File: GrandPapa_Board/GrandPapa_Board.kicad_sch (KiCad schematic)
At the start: 0 parts

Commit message: Shameless papa copying pt 1
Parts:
- added J? (x3): M80-5000642, Payload2020_custom:connector_Harwin_M80-5000642, symbol Connector_Generic:Conn_02x03_Counter_Clockwise
- added J?: Conn_02x06, Connector_PinHeader_2.54mm:PinHeader_1x05_P2.54mm_Vertical, symbol Connector:Conn_01x05_Female
- added J?: Conn_01x02_Female, symbol Connector:Conn_01x02_Female
- added J?: Conn_02x06, Payload2020_custom:connector_Harwin_M80-5000642, symbol Connector_Generic:Conn_01x05
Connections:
- new net +3V3: J?.4 (Pin_4)
- new net CANH_PAYLOAD: J?.4 (Pin_4), J?.4 (Pin_4), J?.4 (Pin_4)
- new net CANH_ROCKET: J?.4 (Pin_4)
- new net CANL_PAYLOAD: J?.5 (Pin_5), J?.5 (Pin_5), J?.5 (Pin_5)
- new net CANL_ROCKET: J?.5 (Pin_5)
- new net GND: J?.3 (Pin_3), J?.3 (Pin_3), J?.3 (Pin_3), J?.3 (Pin_3), J?.3 (Pin_3)
- new net ICSPCLK: J?.1 (Pin_1)
- new net ICSPDAT: J?.2 (Pin_2)
- new net ~{MCLR}: J?.5 (Pin_5)
- no-connect marks 0 -> 5
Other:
- note added: "Connector for programming"
- note added: "GPS Board"
- note added: "Harwin connector"
- note added: "Logger Board"
- note added: "Minisesnor Board"
- note added: "Motor CTRL"
- note added: "Normal header"
- note added: "To Rocket CAN bus"

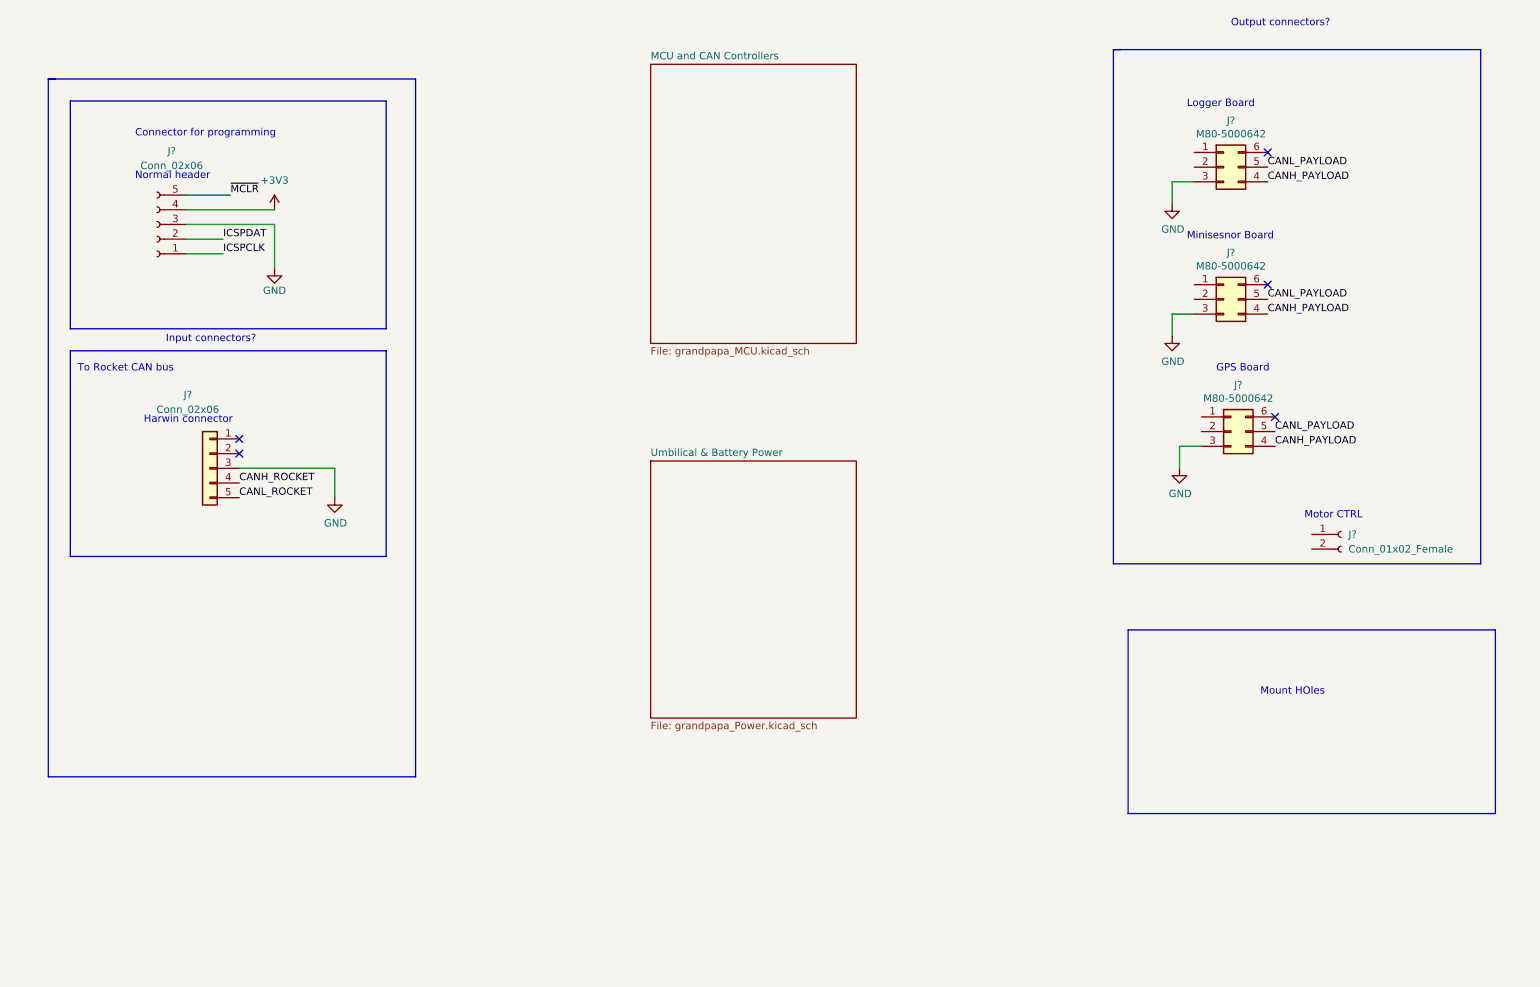
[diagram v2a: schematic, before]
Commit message: Add missing capacitor value, annotate symbols
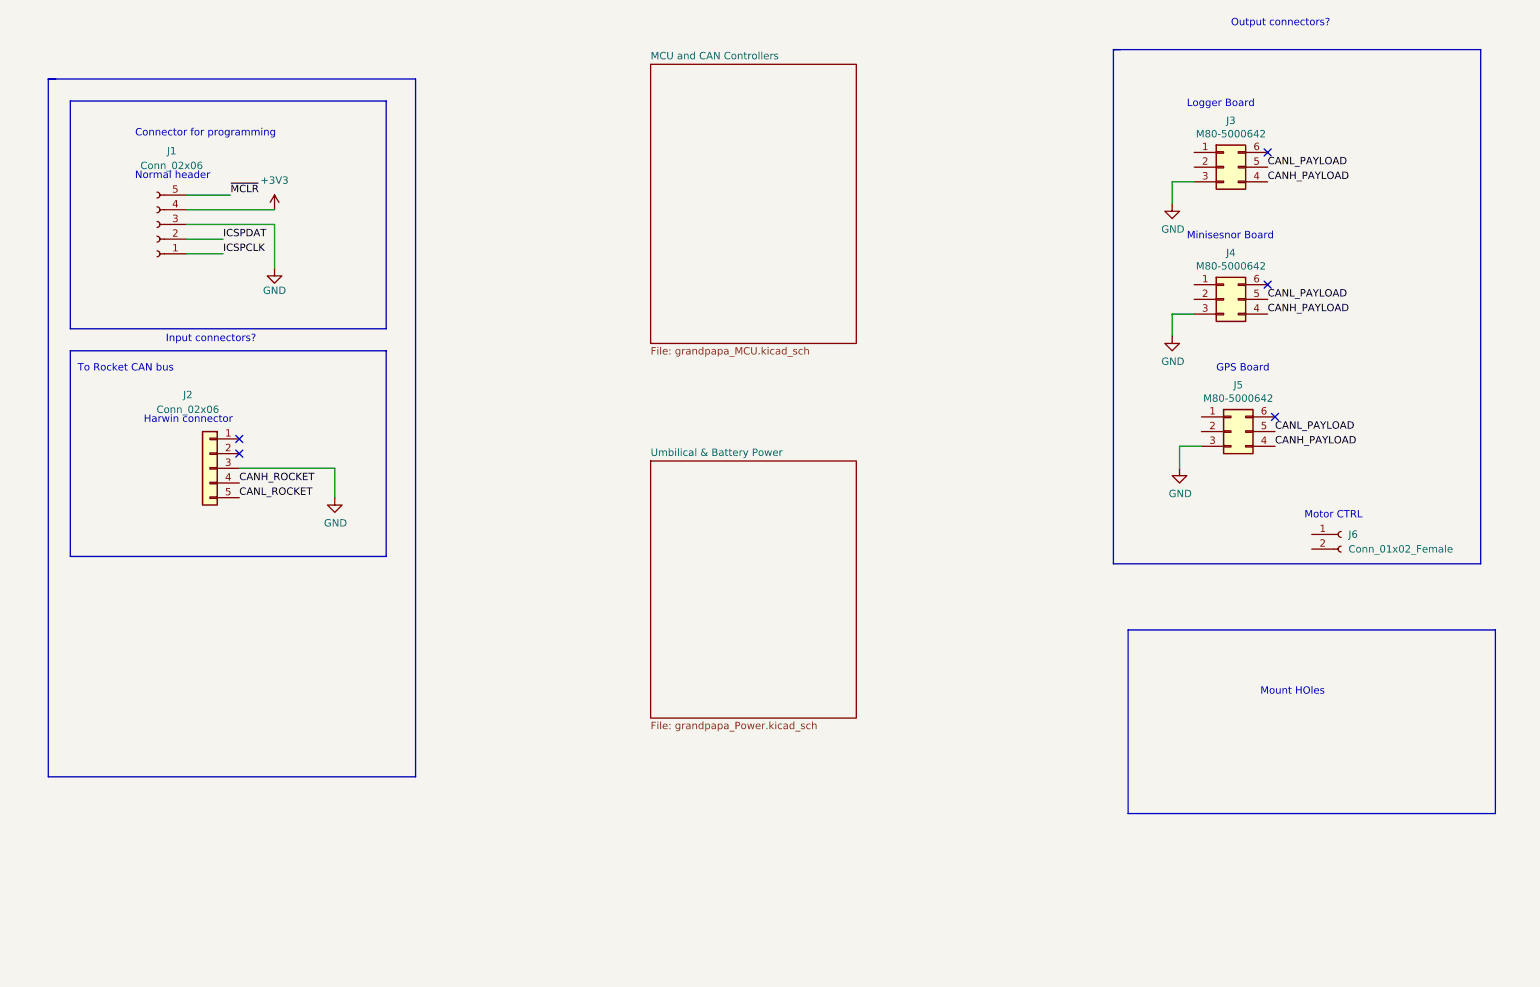
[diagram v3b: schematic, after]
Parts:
- gave numbers to parts that had none: 6

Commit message: Add motor current sense amp and board output connections
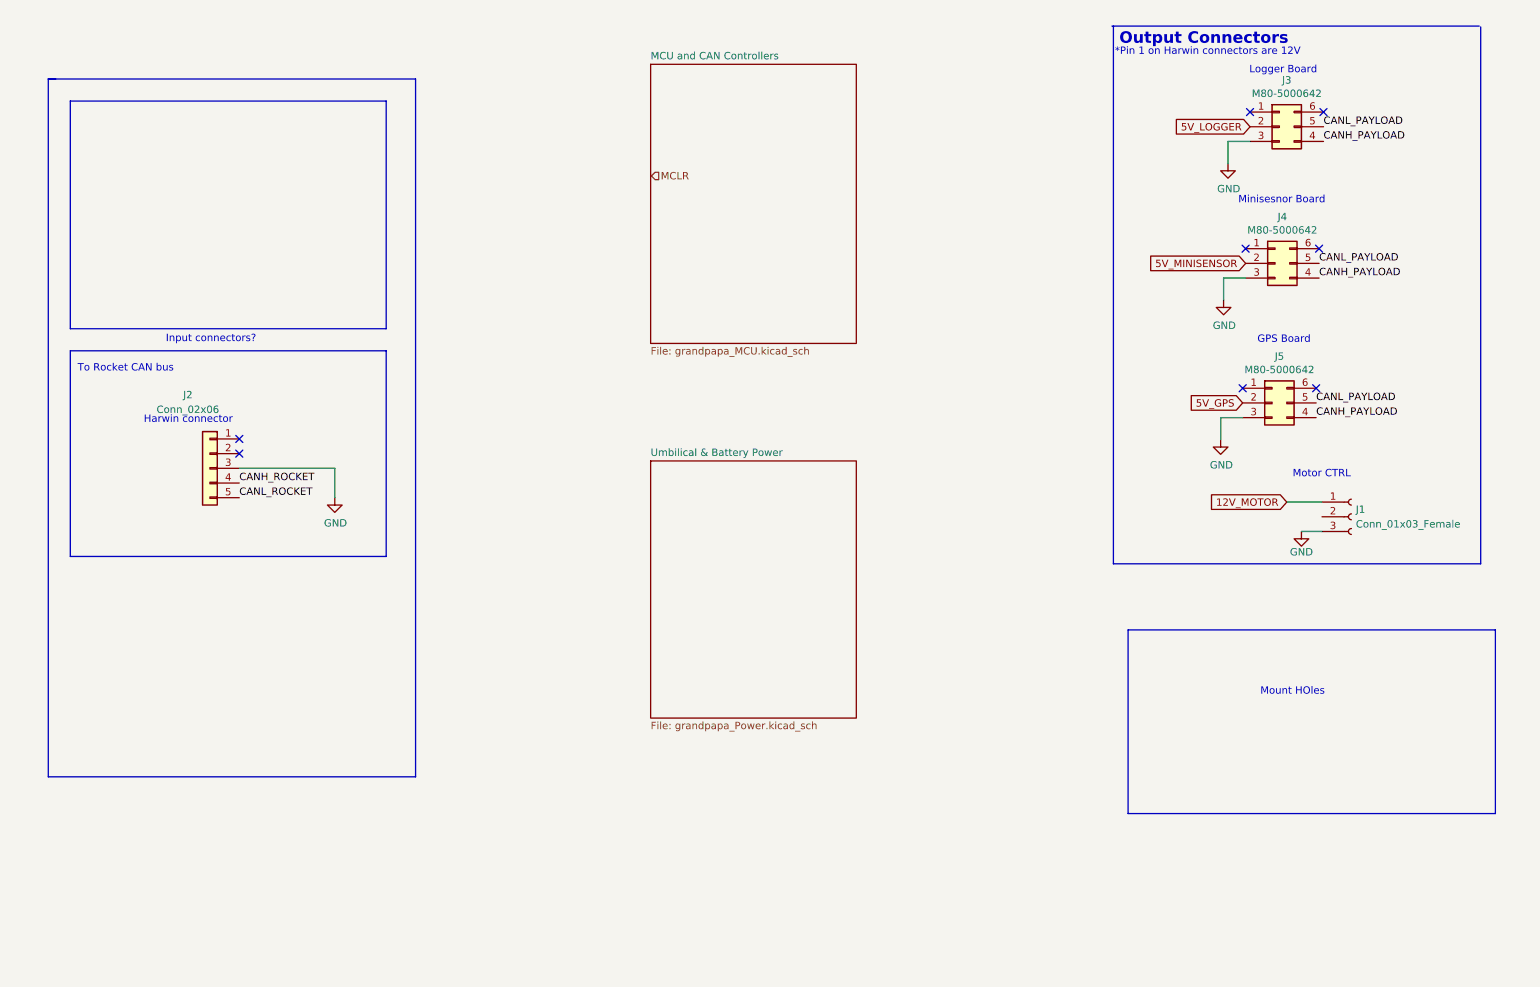
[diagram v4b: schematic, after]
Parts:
- removed J1: Conn_02x06, Connector_PinHeader_2.54mm:PinHeader_1x05_P2.54mm_Vertical, symbol Connector:Conn_01x05_Female
- removed J6: Conn_01x02_Female, symbol Connector:Conn_01x02_Female
- added J1: Conn_01x03_Female, symbol Connector:Conn_01x03_Female
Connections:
- net GND: now also J1.3 (Pin_3)
- net 5V_LOGGER: now reaches J3.2 (Pin_2)
- net 5V_GPS: now reaches J5.2 (Pin_2)
- net 5V_MINISENSOR: now reaches J4.2 (Pin_2)
- new net 12V_MOTOR: J1.1 (Pin_1)
- no-connect marks 5 -> 8
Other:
- note added: "*Pin 1 on Harwin connectors are 12V"
- note added: "Output Connectors"
- note removed: "Connector for programming"
- note removed: "Normal header"
- note removed: "Output connectors?"
- moved on the sheet: J3, J4, J5

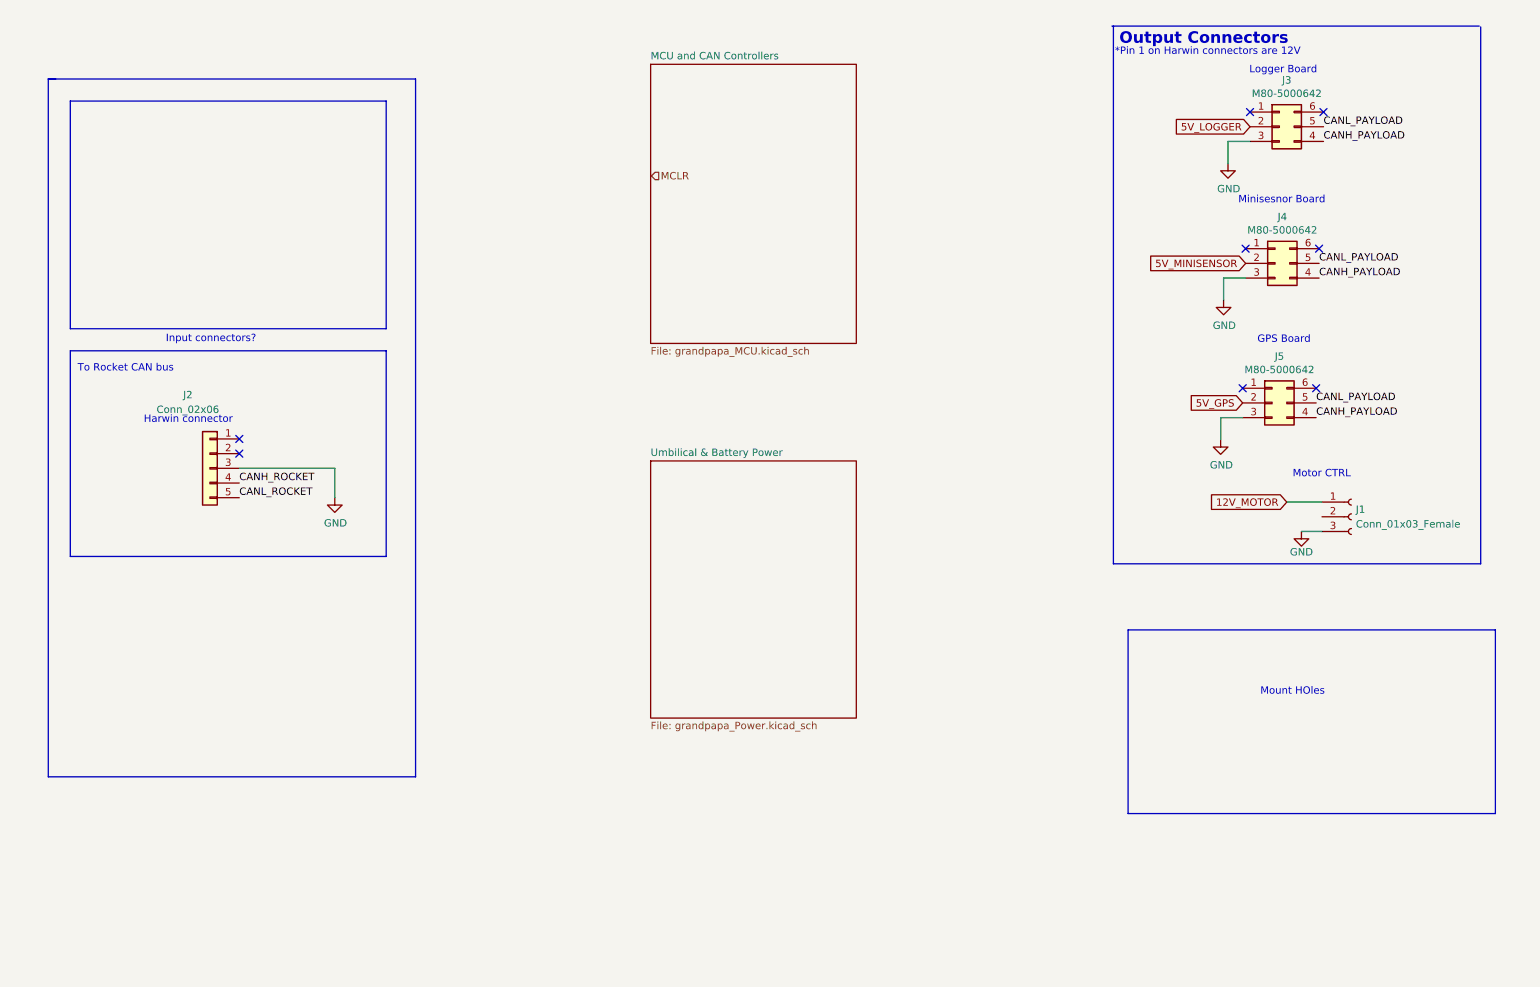
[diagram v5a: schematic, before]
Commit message: Add INA180 to symbol lib, update 5v switch labels
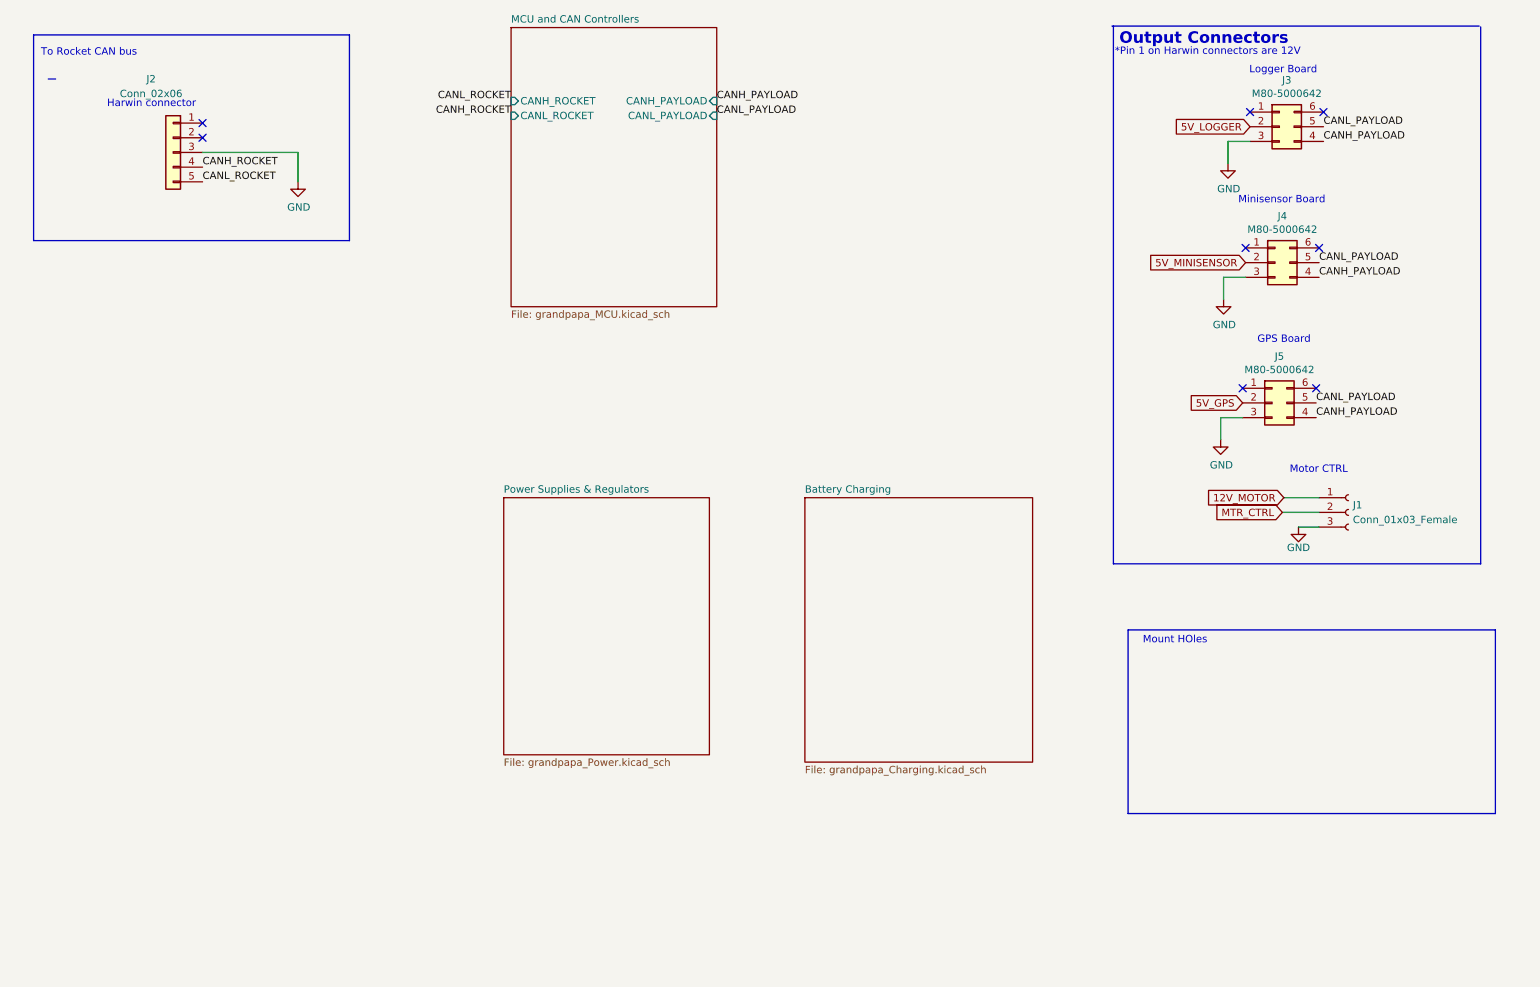
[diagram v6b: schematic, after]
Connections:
- net MTR_CTRL: now reaches J1.2 (Pin_2)
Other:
- sheet Umbilical & Battery Power renamed Power Supplies & Regulators
- added sheet Battery Charging (grandpapa_Charging.kicad_sch)
- sheet MCU and CAN Controllers ports: added CANH_PAYLOAD, CANH_ROCKET, CANL_PAYLOAD, CANL_ROCKET; removed none
- note added: "Minisensor Board"
- note removed: "Input connectors?"
- note removed: "Minisesnor Board"
- moved on the sheet: J1, J2
